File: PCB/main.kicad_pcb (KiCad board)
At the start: 4 copper layers, 65.2 x 45.1 mm, 65 parts, among them J1 S20B-PADSS-1, J2 S20B-PADSS-1, J3 SWD, SW1 Tactile, U1 TPS54302, U2 XC6206P33, U3 TJA1051T/3, U4 TJA1051T/3, U5 STM32G0B1, Y1 40M

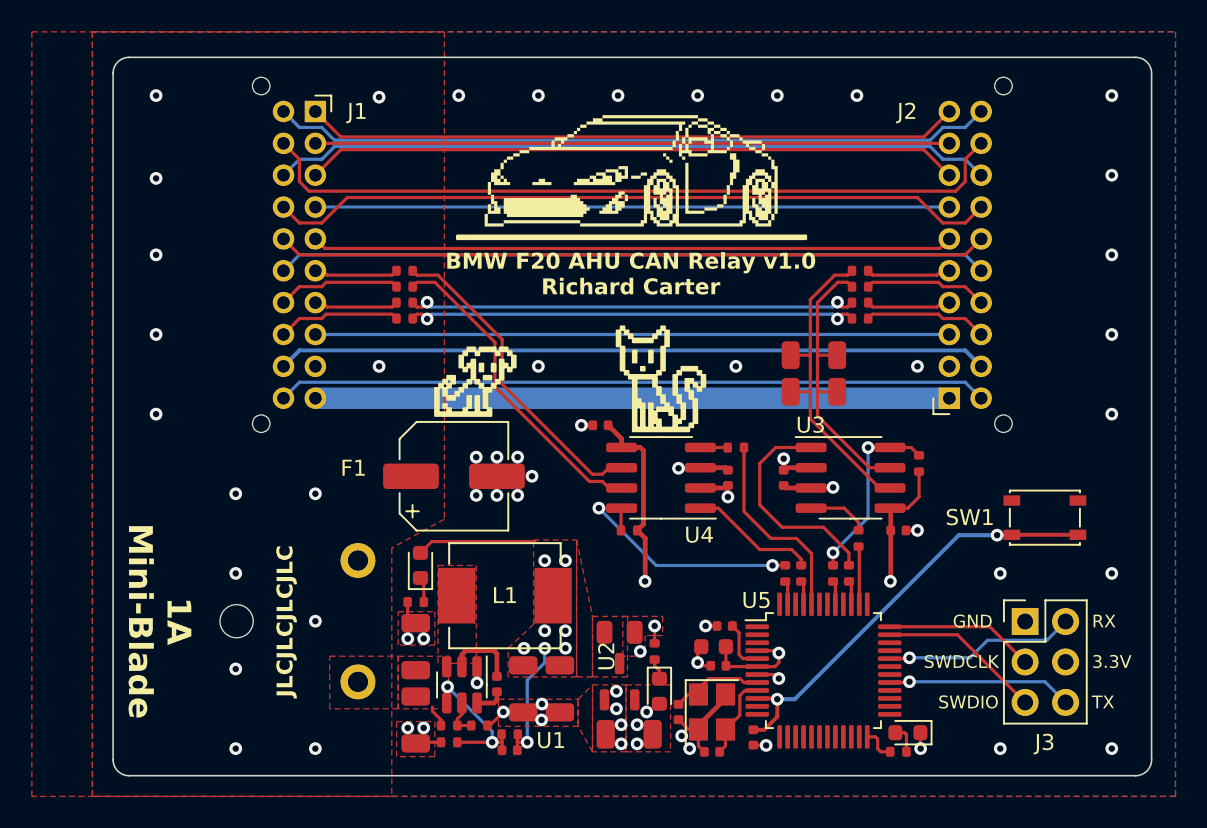
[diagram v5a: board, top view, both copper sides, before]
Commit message: Add boss hole incase I need to use B20B-PADSS-1F
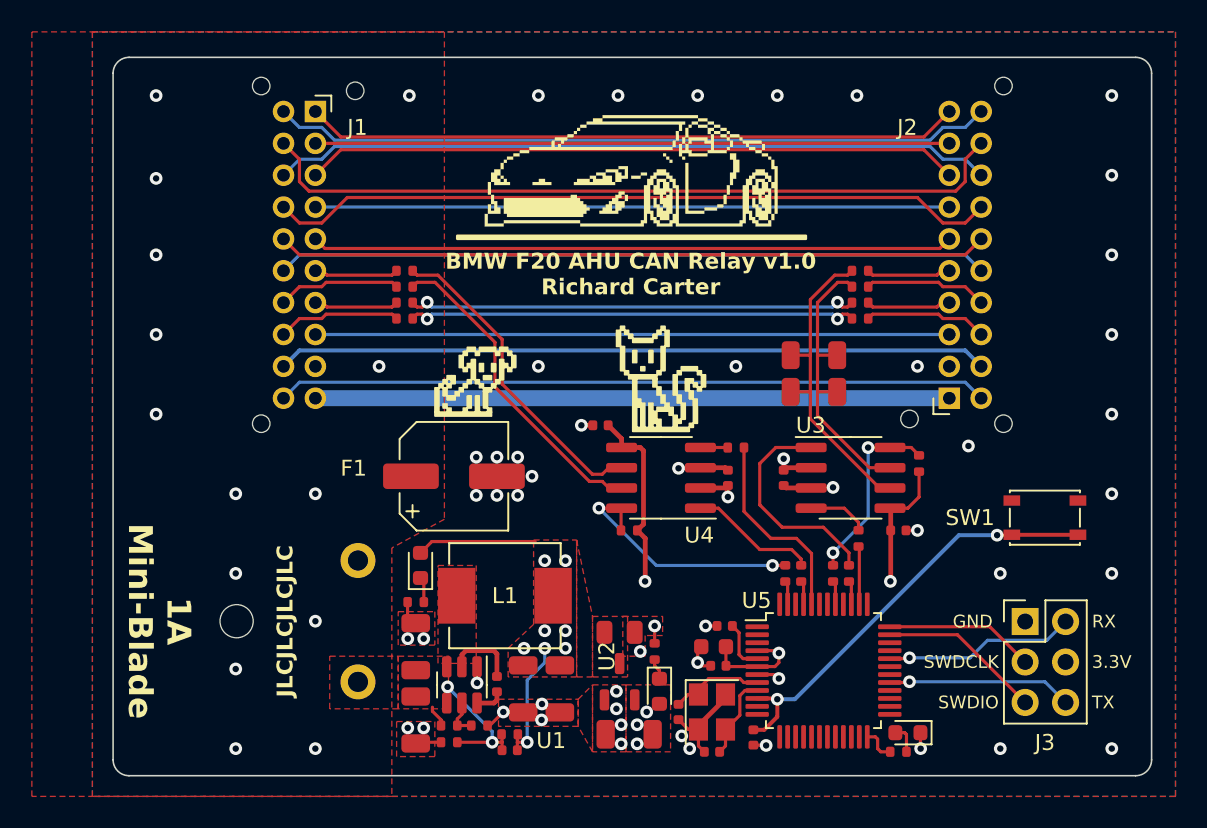
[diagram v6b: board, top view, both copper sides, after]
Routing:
- net GND: vias 64 -> 65
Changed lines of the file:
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@@
     (property "ki_keywords" "connector")
     (attr through_hole)
-    (fp_text reference "J2" (at 2 18 180) (layer "F.SilkS")
+    (fp_text reference "J2" (at 2 17 180) (layer "F.SilkS")
         (effects (font (size 1 1) (thickness 0.15)) (justify right))
     )
@@
     (pad "" np_thru_hole circle (at -3.4 -1.6 180) (size 1.1 1.1) (drill 1.1) (layers "F&B.Cu" "*.Mask"))
     (pad "" np_thru_hole circle (at -3.4 19.6 180) (size 1.1 1.1) (drill 1.1) (layers "F&B.Cu" "*.Mask"))
+    (pad "" np_thru_hole circle (at 2.5 -1.3 180) (size 1.1 1.1) (drill 1.1) (layers "F&B.Cu" "*.Mask"))
     (pad "1" thru_hole rect (at 0 0 180) (size 1.35 1.35) (drill 0.8) (layers "*.Cu" "*.Mask")
       (net 61 "/JST_10_BAT+") (pinfunction "Pin_1") (pintype "passive"))
@@
     (property "ki_keywords" "connector")
     (attr through_hole)
-    (fp_text reference "J1" (at 2 0) (layer "F.SilkS")
+    (fp_text reference "J1" (at 2 1) (layer "F.SilkS")
         (effects (font (size 1 1) (thickness 0.15)) (justify left))
     )
@@
     (pad "" np_thru_hole circle (at -3.4 -1.6) (size 1.1 1.1) (drill 1.1) (layers "F&B.Cu" "*.Mask"))
     (pad "" np_thru_hole circle (at -3.4 19.6) (size 1.1 1.1) (drill 1.1) (layers "F&B.Cu" "*.Mask"))
+    (pad "" np_thru_hole circle (at 2.5 -1.3) (size 1.1 1.1) (drill 1.1) (layers "F&B.Cu" "*.Mask"))
     (pad "1" thru_hole rect (at 0 0) (size 1.35 1.35) (drill 0.8) (layers "*.Cu" "*.Mask")
       (net 9 "/JST_01_AUX_IN") (pinfunction "Pin_1") (pintype "passive"))
@@
   (segment (start 69.65 59.66) (end 69.65 60.9375) (width 0.2) (layer "F.Cu") (net 57))
   (segment (start 69.5 59.51) (end 69.65 59.66) (width 0.2) (layer "F.Cu") (net 57))
-  (segment (start 40 48) (end 79.8 48) (width 1.35) (layer "B.Cu") (net 61))
+  (segment (start 79.8 48) (end 40 48) (width 1) (layer "B.Cu") (net 61))
   (segment (start 66.9 65.85) (end 66.65 65.6) (width 0.2) (layer "F.Cu") (net 62))
   (segment (start 64.7 65.6) (end 64.05 66.25) (width 0.2) (layer "F.Cu") (net 62))
@@
   (via (at 30 29) (size 0.8) (drill 0.4) (layers "F.Cu" "B.Cu") (net 81))
   (via (at 54.2 68.2) (size 0.8) (drill 0.4) (layers "F.Cu" "B.Cu") (free) (net 81))
-  (via (at 49 29) (size 0.8) (drill 0.4) (layers "F.Cu" "B.Cu") (net 81))
+  (via (at 45.9 29) (size 0.8) (drill 0.4) (layers "F.Cu" "B.Cu") (net 81))
   (via (at 52.7 54.1) (size 0.8) (drill 0.4) (layers "F.Cu" "B.Cu") (free) (net 81))
   (via (at 78 70) (size 0.8) (drill 0.4) (layers "F.Cu" "B.Cu") (net 81))
@@
   (via (at 30 34.2) (size 0.8) (drill 0.4) (layers "F.Cu" "B.Cu") (net 81))
   (via (at 46.8 68.7) (size 0.8) (drill 0.4) (layers "F.Cu" "B.Cu") (free) (net 81))
+  (via (at 90 54) (size 0.8) (drill 0.4) (layers "F.Cu" "B.Cu") (net 81))
   (via (at 90 49) (size 0.8) (drill 0.4) (layers "F.Cu" "B.Cu") (net 81))
   (via (at 54.225 67.2) (size 0.8) (drill 0.4) (layers "F.Cu" "B.Cu") (free) (net 81))
+  (via (at 81 51) (size 0.8) (drill 0.4) (layers "F.Cu" "B.Cu") (net 81))
   (via (at 77.8 46) (size 0.8) (drill 0.4) (layers "F.Cu" "B.Cu") (free) (net 81))
   (via (at 54 29) (size 0.8) (drill 0.4) (layers "F.Cu" "B.Cu") (net 81))
@@
   (via (at 59.2 69.7) (size 0.8) (drill 0.4) (layers "F.Cu" "B.Cu") (free) (net 81))
   (via (at 63 69.2) (size 0.8) (drill 0.4) (layers "F.Cu" "B.Cu") (free) (net 81))
-  (via (at 44 29.1) (size 0.8) (drill 0.4) (layers "F.Cu" "B.Cu") (net 81))
   (via (at 58.9 67.5) (size 0.8) (drill 0.4) (layers "F.Cu" "B.Cu") (free) (net 81))
   (via (at 45.8 63.1) (size 0.8) (drill 0.4) (layers "F.Cu" "B.Cu") (free) (net 81))

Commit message: Change fuse and adjust board size
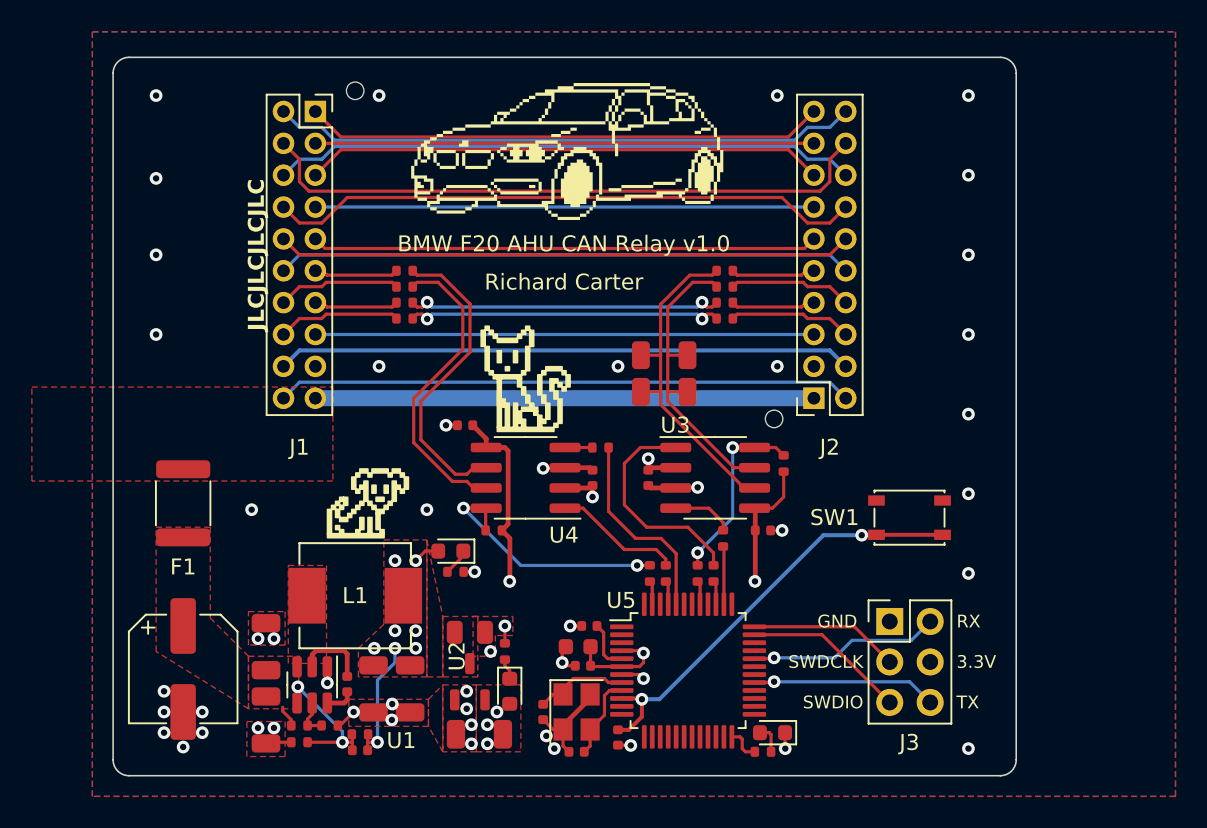
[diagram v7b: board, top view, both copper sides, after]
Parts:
- added ?: , clipboard:bd69859f-0a0a-4dc6-8e34-8240c4a665a7, F.Cu at (68.8, 49.3)
- added ?: , clipboard:bd69859f-0a0a-4dc6-8e34-8240c4a665a7, F.Cu at (42.5, 28.7)
- F1: value Fuse -> 500mA; footprint libdb:CMP-0026 -> libdb:CMP-0076
- J1, J2: footprint libdb:CMP-0012 -> libdb:CMP-0074
- REF**: value CMP-0066 -> CMP-0077; footprint libdb:CMP-0066 -> libdb:CMP-0077
- moved ART3 23.2 mm to (36.3, 38.9)
- moved C19 20.9 mm to (31.7, 65.0), turned to -90 degrees
- moved REF** 10.2 mm to (43.6, 55.2)
- moved C4 9.40 mm to (42.8, 70.1)
- moved C8 9.40 mm to (50.3, 69.1)
- moved R3 9.40 mm to (42.8, 69.1)
- moved U1 9.40 mm to (39.8, 66.0)
- moved C1 9.40 mm to (36.9, 68.2)
- moved C2 9.40 mm to (36.9, 63.6)
- moved C3 9.40 mm to (42.0, 66.0)
- moved C5 9.40 mm to (46.0, 66.2)
- moved C6 9.40 mm to (43.6, 66.2)
- moved C7 9.40 mm to (49.7, 62.7)
- moved D2 9.40 mm to (52.2, 66.4)
- moved L1 9.40 mm to (42.5, 60.4)
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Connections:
- C19 pad 1: /JST_10_BAT+ -> +BATT
- F1 pad 1: /JST_10_BAT+ -> +BATT
- F1 pad 2: +BATT -> /JST_10_BAT+
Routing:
- net /JST_05_BK_VID_IN: track 40.3 -> 31.8 mm
- net /JST_16_NC: track 44.6 -> 36.1 mm
- net /JST_13_AUDIO_FL: track 45.3 -> 36.8 mm
- net /JST_12_AUDIO_FL: track 47.9 -> 39.4 mm
- net /JST_11_AUDIO_FL: track 45.3 -> 36.8 mm
- net /JST_10_BAT+: track 39.8 -> 31.3 mm
- net /JST_08_CAM_DET: track 39.8 -> 31.3 mm
- net /JST_04_NC: track 39.8 -> 31.3 mm
- net /JST_03_AUX_IN: track 41.1 -> 32.6 mm
- net /JST_02_AUX_IN: track 39.8 -> 31.3 mm
- net /JST_01_AUX_IN: track 41.1 -> 32.6 mm
- net /FW_CAN2-: track 28.3 -> 19.8 mm
- net /FW_CAN2+: track 28.3 -> 19.8 mm
- net /JST_20_NC: track 44.6 -> 36.1 mm
- net /JST_19_CAM_12V+: track 44.6 -> 36.1 mm
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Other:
- board size 65.2 x 45.1 mm -> 56.7 x 45.1 mm
- board text added: "BMW F20 AHU CAN Relay v1.0"
- board text added: "Richard Carter"
- board text removed: "1A Mini-Blade"
- board text removed: "BMW F20 AHU CAN Relay v1.0 Richard Carter"

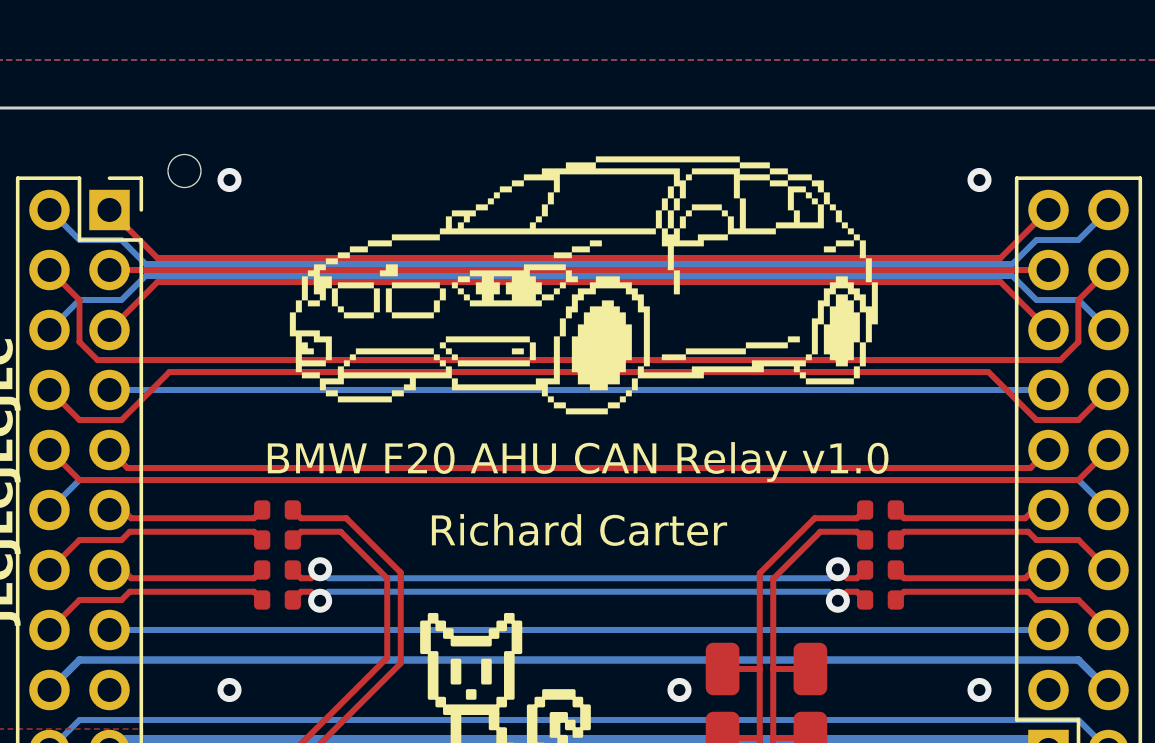
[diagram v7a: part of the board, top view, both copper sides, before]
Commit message: Update car graphic
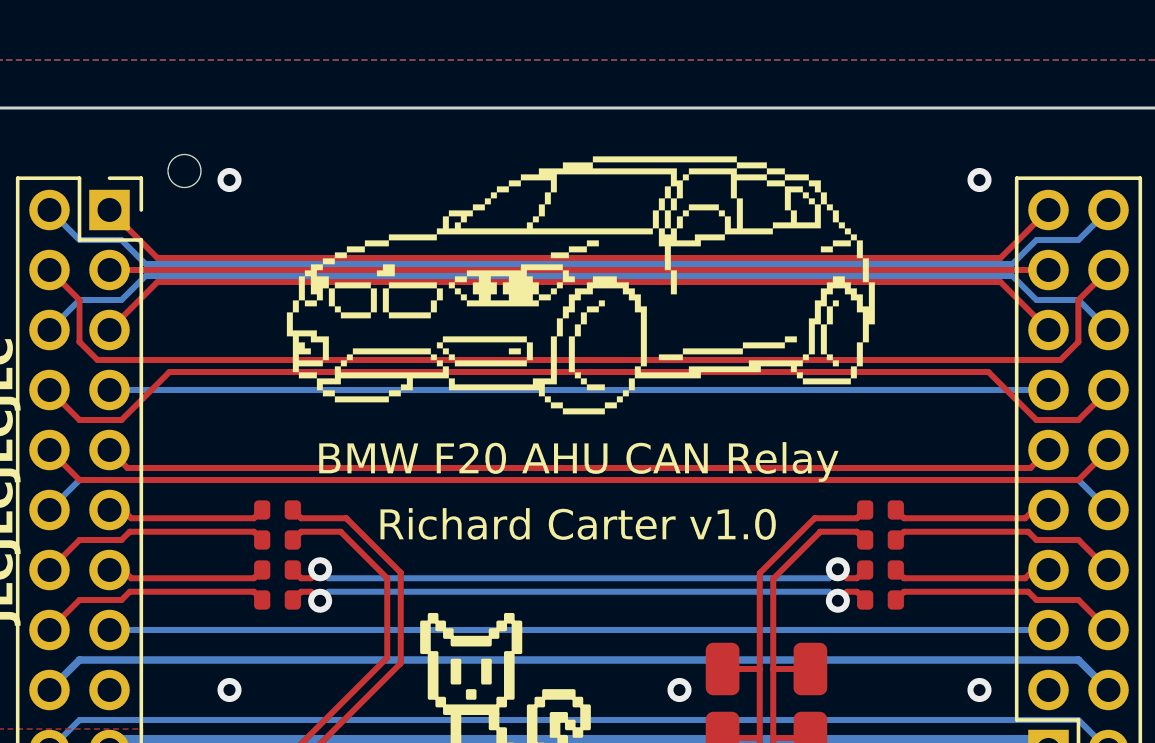
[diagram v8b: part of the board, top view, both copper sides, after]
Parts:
- moved REF** 0.10 mm to (45.7, 28.0)
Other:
- board text added: "BMW F20 AHU CAN Relay"
- board text added: "Richard Carter v1.0"
- board text removed: "BMW F20 AHU CAN Relay v1.0"
- board text removed: "Richard Carter"
